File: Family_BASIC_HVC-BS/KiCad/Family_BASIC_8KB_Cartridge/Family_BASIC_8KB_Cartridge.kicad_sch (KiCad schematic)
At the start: 21 parts, among them IC1 Working RAM (62256), IC3 74HCT20, IC4 Character ROM (2764), SW1 BACKUP SW, SW2 RAM BANK SW, SW3 A_{15} SW, U1 Program ROM (27512)

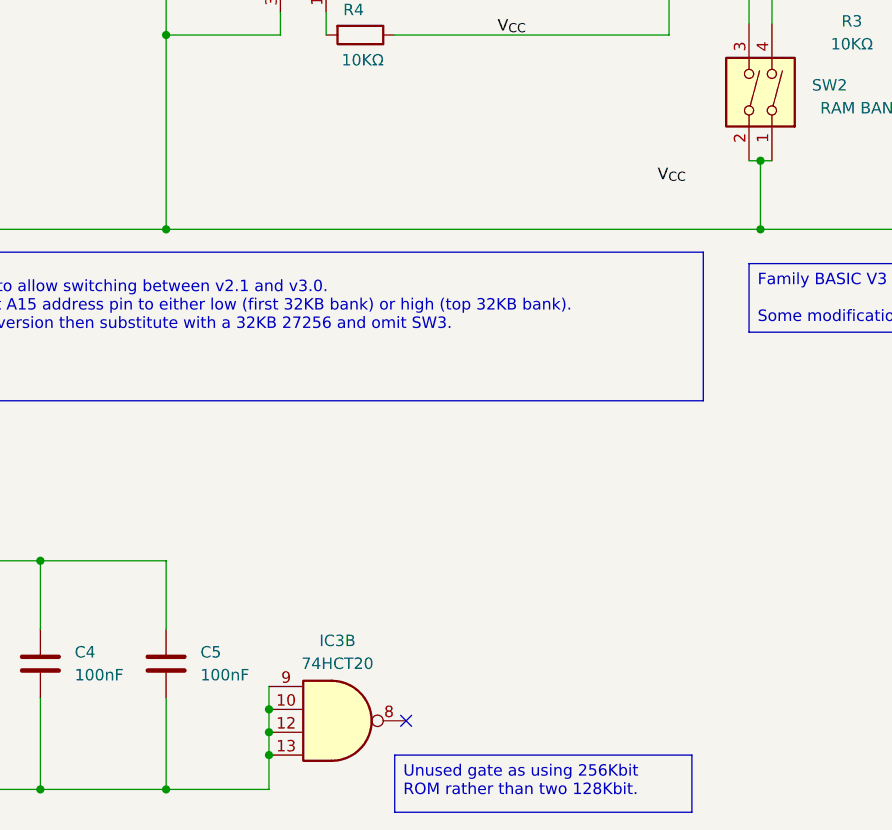
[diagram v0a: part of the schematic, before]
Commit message: Reorganised KiCad folders
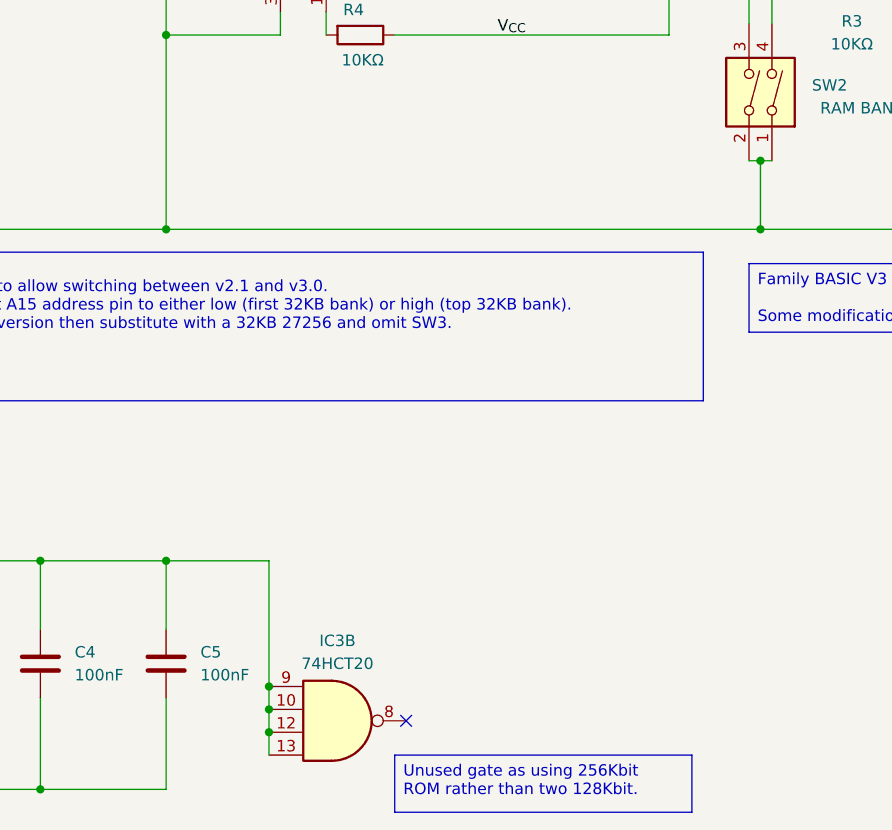
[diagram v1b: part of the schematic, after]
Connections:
- net GND: no longer IC3.10, IC3.12, IC3.13, IC3.9
- net V_{CC}: now also IC3.10, IC3.12, IC3.13, IC3.9
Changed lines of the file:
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@@
 	)
 	(junction
-		(at 113.03 189.23)
+		(at 243.84 86.36)
 		(diameter 0)
 		(color 0 0 0 0)
 	)
 	(junction
-		(at 243.84 86.36)
+		(at 113.03 184.15)
 		(diameter 0)
 		(color 0 0 0 0)
@@
 	)
 	(junction
-		(at 101.6 193.04)
+		(at 113.03 186.69)
 		(diameter 0)
 		(color 0 0 0 0)
@@
 	)
 	(junction
-		(at 232.41 130.81)
+		(at 113.03 181.61)
 		(diameter 0)
 		(color 0 0 0 0)
 	)
 	(junction
-		(at 73.66 193.04)
+		(at 101.6 167.64)
 		(diameter 0)
 		(color 0 0 0 0)
 	)
 	(junction
-		(at 113.03 186.69)
+		(at 232.41 130.81)
+		(diameter 0)
+		(color 0 0 0 0)
+	)
+	(junction
+		(at 73.66 193.04)
 		(diameter 0)
 		(color 0 0 0 0)
@@
 	)
 	(junction
-		(at 113.03 184.15)
-		(diameter 0)
-		(color 0 0 0 0)
-	)
-	(junction
 		(at 167.64 123.19)
 		(diameter 0)
@@
 	(wire
 		(pts
-			(xy 205.74 99.06) (xy 205.74 104.14)
+			(xy 113.03 181.61) (xy 113.03 184.15)
 		)
 		(stroke
@@
 		)
 	)
-	(bus
+	(wire
 		(pts
-			(xy 20.32 81.28) (xy 20.32 86.36)
+			(xy 205.74 99.06) (xy 205.74 104.14)
 		)
 		(stroke
@@
 	(bus
 		(pts
-			(xy 215.9 50.8) (xy 215.9 53.34)
+			(xy 20.32 81.28) (xy 20.32 86.36)
 		)
 		(stroke
@@
 		)
 	)
-	(wire
+	(bus
 		(pts
-			(xy 113.03 186.69) (xy 113.03 189.23)
+			(xy 215.9 50.8) (xy 215.9 53.34)
 		)
 		(stroke
@@
 	(wire
 		(pts
+			(xy 113.03 186.69) (xy 113.03 189.23)
+		)
+		(stroke
+			(width 0)
+			(type default)
+		)
+	)
+	(wire
+		(pts
+			(xy 101.6 167.64) (xy 113.03 167.64)
+		)
+		(stroke
+			(width 0)
+			(type default)
+		)
+	)
+	(wire
+		(pts
 			(xy 246.38 58.42) (xy 250.19 58.42)
 		)
@@
 	(wire
 		(pts
-			(xy 113.03 184.15) (xy 113.03 186.69)
-		)
-		(stroke
-			(width 0)
-			(type default)
-		)
-	)
-	(wire
-		(pts
 			(xy 205.74 130.81) (xy 232.41 130.81)
 		)
@@
 	(wire
 		(pts
-			(xy 113.03 193.04) (xy 113.03 189.23)
-		)
-		(stroke
-			(width 0)
-			(type default)
-		)
-	)
-	(wire
-		(pts
 			(xy 101.6 96.52) (xy 101.6 109.22)
 		)
@@
 		)
 	)
-	(wire
-		(pts
-			(xy 101.6 193.04) (xy 113.03 193.04)
-		)
-		(stroke
-			(width 0)
-			(type default)
-		)
-	)
 	(bus
 		(pts
@@
 	(wire
 		(pts
+			(xy 113.03 167.64) (xy 113.03 181.61)
+		)
+		(stroke
+			(width 0)
+			(type default)
+		)
+	)
+	(wire
+		(pts
 			(xy 205.74 123.19) (xy 205.74 130.81)
 		)
@@
 		)
 	)
-	(wire
-		(pts
-			(xy 113.03 181.61) (xy 113.03 184.15)
-		)
-		(stroke
-			(width 0)
-			(type default)
-		)
-	)
 	(bus
 		(pts
@@
 	(wire
 		(pts
+			(xy 113.03 184.15) (xy 113.03 186.69)
+		)
+		(stroke
+			(width 0)
+			(type default)
+		)
+	)
+	(wire
+		(pts
 			(xy 81.28 63.5) (xy 91.44 63.5)
 		)
@@
 		(effects
 			(font
-				(size 1.27 1.27)
-			)
-			(justify left bottom)
-		)
-	)
-	(label "V_{CC}"
-		(at 156.21 125.73 0)
-		(effects
-			(font
